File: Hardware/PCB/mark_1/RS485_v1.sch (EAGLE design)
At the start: 4 parts

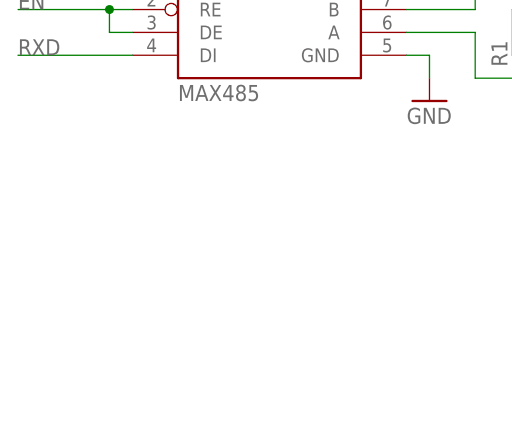
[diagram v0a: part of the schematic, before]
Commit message: 
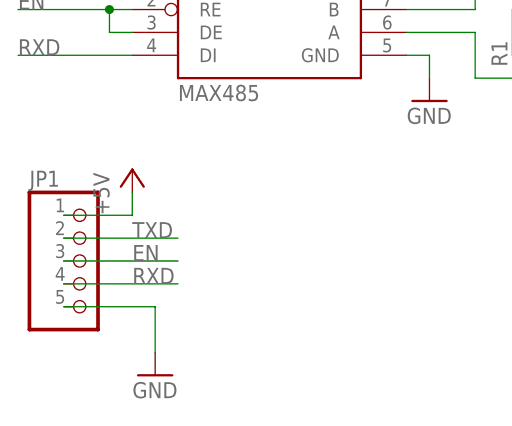
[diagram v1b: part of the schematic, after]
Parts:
- added JP1: (no value), mark_1:PINHD-1X5
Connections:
- net +5V: now also JP1.1
- net EN: now also JP1.3
- net GND: now also JP1.5
- net RXD: now also JP1.4
- net TXD: now also JP1.2
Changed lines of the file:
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@@
 <part name="C1" library="mark_1" deviceset="C-EU" device="C0805K" value="100nF"/>
 <part name="GND3" library="mark_1" deviceset="GND" device=""/>
+<part name="JP1" library="mark_1" deviceset="PINHD-1X5" device=""/>
+<part name="P+3" library="mark_1" deviceset="+5V" device=""/>
+<part name="GND4" library="mark_1" deviceset="GND" device=""/>
 </parts>
 <sheets>
@@
 <instance part="C1" gate="G$1" x="96.52" y="25.4"/>
 <instance part="GND3" gate="1" x="96.52" y="15.24"/>
+<instance part="JP1" gate="A" x="22.86" y="-2.54"/>
+<instance part="P+3" gate="1" x="27.94" y="7.62"/>
+<instance part="GND4" gate="1" x="30.48" y="-15.24"/>
 </instances>
 <busses>
@@
 <pinref part="C1" gate="G$1" pin="1"/>
 <wire x1="96.52" y1="30.48" x2="96.52" y2="27.94" width="0.1524" layer="91"/>
+</segment>
+<segment>
+<pinref part="P+3" gate="1" pin="+5V"/>
+<wire x1="27.94" y1="5.08" x2="27.94" y2="2.54" width="0.1524" layer="91"/>
+<pinref part="JP1" gate="A" pin="1"/>
+<wire x1="27.94" y1="2.54" x2="20.32" y2="2.54" width="0.1524" layer="91"/>
 </segment>
 </net>
@@
 <wire x1="96.52" y1="20.32" x2="96.52" y2="17.78" width="0.1524" layer="91"/>
 </segment>
+<segment>
+<pinref part="JP1" gate="A" pin="5"/>
+<pinref part="GND4" gate="1" pin="GND"/>
+<wire x1="20.32" y1="-7.62" x2="30.48" y2="-7.62" width="0.1524" layer="91"/>
+<wire x1="30.48" y1="-7.62" x2="30.48" y2="-12.7" width="0.1524" layer="91"/>
+</segment>
 </net>
 <net name="TXD" class="0">
@@
 <label x="15.24" y="27.94" size="1.778" layer="95"/>
 </segment>
+<segment>
+<pinref part="JP1" gate="A" pin="2"/>
+<wire x1="20.32" y1="0" x2="33.02" y2="0" width="0.1524" layer="91"/>
+<label x="27.94" y="0" size="1.778" layer="95"/>
+</segment>
 </net>
 <net name="RXD" class="0">
@@
 <wire x1="27.94" y1="20.32" x2="15.24" y2="20.32" width="0.1524" layer="91"/>
 <label x="15.24" y="20.32" size="1.778" layer="95"/>
+</segment>
+<segment>
+<pinref part="JP1" gate="A" pin="4"/>
+<wire x1="20.32" y1="-5.08" x2="33.02" y2="-5.08" width="0.1524" layer="91"/>
+<label x="27.94" y="-5.08" size="1.778" layer="95"/>
 </segment>
 </net>
@@
 <label x="15.24" y="25.4" size="1.778" layer="95"/>
 </segment>
+<segment>
+<pinref part="JP1" gate="A" pin="3"/>
+<wire x1="20.32" y1="-2.54" x2="33.02" y2="-2.54" width="0.1524" layer="91"/>
+<label x="27.94" y="-2.54" size="1.778" layer="95"/>
+</segment>
 </net>

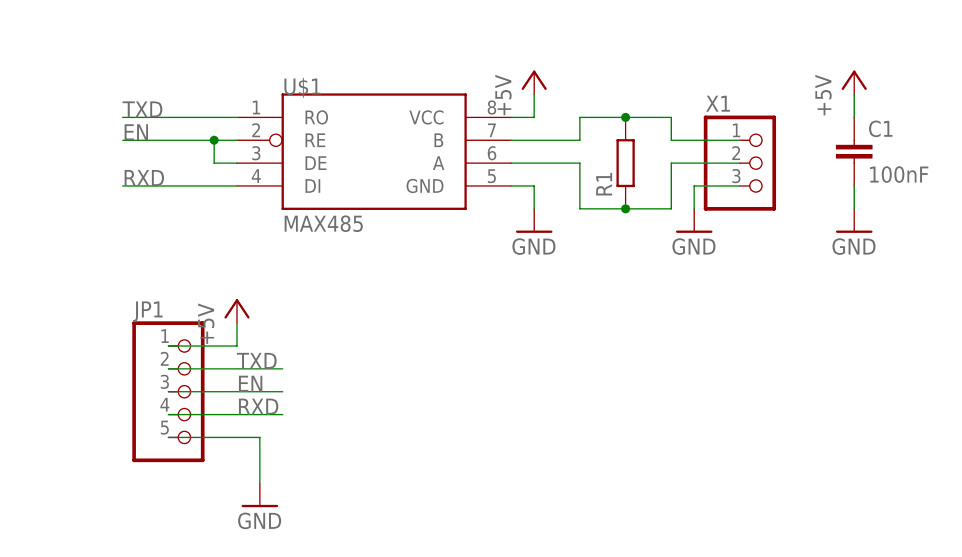
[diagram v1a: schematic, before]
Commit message: 
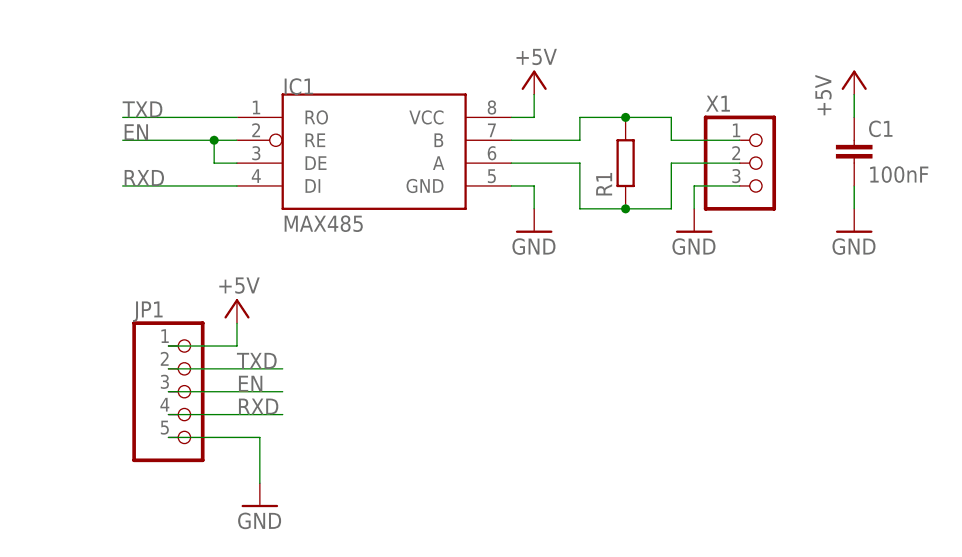
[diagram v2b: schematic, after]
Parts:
- renumbered U$1 to IC1
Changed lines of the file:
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@@
 <part name="P+1" library="mark_1" deviceset="+5V" device=""/>
 <part name="GND1" library="mark_1" deviceset="GND" device=""/>
-<part name="U$1" library="mark_1" deviceset="MAX485" device=""/>
+<part name="IC1" library="mark_1" deviceset="MAX485" device=""/>
 <part name="R1" library="mark_1" deviceset="R-EU_" device="R0805"/>
 <part name="X1" library="mark_1" deviceset="W237-103" device=""/>
@@
 </plain>
 <instances>
-<instance part="P+1" gate="1" x="60.96" y="33.02"/>
+<instance part="P+1" gate="1" x="60.96" y="33.02" smashed="yes">
+<attribute name="VALUE" x="63.5" y="35.56" size="1.778" layer="96" rot="R180"/>
+</instance>
 <instance part="GND1" gate="1" x="60.96" y="15.24"/>
-<instance part="U$1" gate="G$1" x="43.18" y="22.86"/>
+<instance part="IC1" gate="G$1" x="43.18" y="22.86"/>
 <instance part="R1" gate="G$1" x="71.12" y="22.86" rot="R90"/>
 <instance part="X1" gate="G$1" x="86.36" y="22.86"/>
@@
 <instance part="GND3" gate="1" x="96.52" y="15.24"/>
 <instance part="JP1" gate="A" x="22.86" y="-2.54"/>
-<instance part="P+3" gate="1" x="27.94" y="7.62"/>
+<instance part="P+3" gate="1" x="27.94" y="7.62" smashed="yes">
+<attribute name="VALUE" x="30.48" y="10.16" size="1.778" layer="96" rot="R180"/>
+</instance>
 <instance part="GND4" gate="1" x="30.48" y="-15.24"/>
 </instances>
@@
 <net name="+5V" class="0">
 <segment>
-<pinref part="U$1" gate="G$1" pin="VCC"/>
+<pinref part="IC1" gate="G$1" pin="VCC"/>
 <pinref part="P+1" gate="1" pin="+5V"/>
 <wire x1="60.96" y1="30.48" x2="60.96" y2="27.94" width="0.1524" layer="91"/>
@@
 <net name="GND" class="0">
 <segment>
-<pinref part="U$1" gate="G$1" pin="GND"/>
+<pinref part="IC1" gate="G$1" pin="GND"/>
 <pinref part="GND1" gate="1" pin="GND"/>
 <wire x1="60.96" y1="17.78" x2="60.96" y2="20.32" width="0.1524" layer="91"/>
@@
 <net name="TXD" class="0">
 <segment>
-<pinref part="U$1" gate="G$1" pin="RO"/>
+<pinref part="IC1" gate="G$1" pin="RO"/>
 <wire x1="27.94" y1="27.94" x2="15.24" y2="27.94" width="0.1524" layer="91"/>
 <label x="15.24" y="27.94" size="1.778" layer="95"/>
@@
 <net name="RXD" class="0">
 <segment>
-<pinref part="U$1" gate="G$1" pin="DI"/>
+<pinref part="IC1" gate="G$1" pin="DI"/>
 <wire x1="27.94" y1="20.32" x2="15.24" y2="20.32" width="0.1524" layer="91"/>
 <label x="15.24" y="20.32" size="1.778" layer="95"/>
@@
 <wire x1="15.24" y1="25.4" x2="25.4" y2="25.4" width="0.1524" layer="91"/>
 <wire x1="25.4" y1="25.4" x2="25.4" y2="22.86" width="0.1524" layer="91"/>
-<pinref part="U$1" gate="G$1" pin="DE"/>
+<pinref part="IC1" gate="G$1" pin="DE"/>
 <wire x1="25.4" y1="22.86" x2="27.94" y2="22.86" width="0.1524" layer="91"/>
 <junction x="25.4" y="25.4"/>
-<pinref part="U$1" gate="G$1" pin="RE"/>
+<pinref part="IC1" gate="G$1" pin="RE"/>
 <wire x1="27.94" y1="25.4" x2="25.4" y2="25.4" width="0.1524" layer="91"/>
 <label x="15.24" y="25.4" size="1.778" layer="95"/>
@@
 <net name="N$1" class="0">
 <segment>
-<pinref part="U$1" gate="G$1" pin="B"/>
+<pinref part="IC1" gate="G$1" pin="B"/>
 <wire x1="58.42" y1="25.4" x2="66.04" y2="25.4" width="0.1524" layer="91"/>
 <wire x1="66.04" y1="25.4" x2="66.04" y2="27.94" width="0.1524" layer="91"/>
@@
 <net name="N$2" class="0">
 <segment>
-<pinref part="U$1" gate="G$1" pin="A"/>
+<pinref part="IC1" gate="G$1" pin="A"/>
 <wire x1="58.42" y1="22.86" x2="66.04" y2="22.86" width="0.1524" layer="91"/>
 <wire x1="66.04" y1="22.86" x2="66.04" y2="17.78" width="0.1524" layer="91"/>

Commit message: 
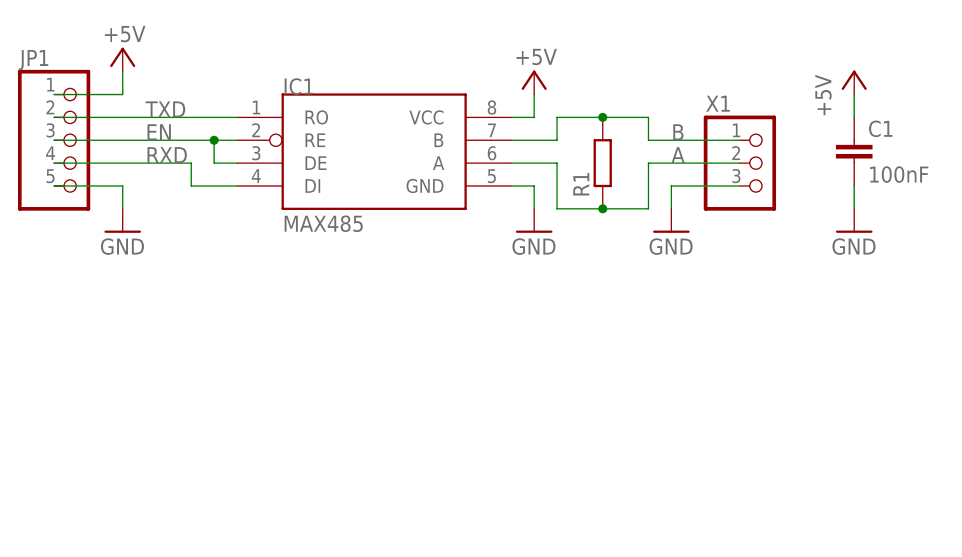
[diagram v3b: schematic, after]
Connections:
- net N$1 renamed B
- net N$2 renamed A
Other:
- moved on the sheet: JP1, R1
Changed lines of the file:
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@@
 <instance part="GND1" gate="1" x="60.96" y="15.24"/>
 <instance part="IC1" gate="G$1" x="43.18" y="22.86"/>
-<instance part="R1" gate="G$1" x="71.12" y="22.86" rot="R90"/>
+<instance part="R1" gate="G$1" x="68.58" y="22.86" rot="R90"/>
 <instance part="X1" gate="G$1" x="86.36" y="22.86"/>
-<instance part="GND2" gate="1" x="78.74" y="15.24"/>
+<instance part="GND2" gate="1" x="76.2" y="15.24"/>
 <instance part="P+2" gate="1" x="96.52" y="33.02"/>
 <instance part="C1" gate="G$1" x="96.52" y="25.4"/>
 <instance part="GND3" gate="1" x="96.52" y="15.24"/>
-<instance part="JP1" gate="A" x="22.86" y="-2.54"/>
-<instance part="P+3" gate="1" x="27.94" y="7.62" smashed="yes">
-<attribute name="VALUE" x="30.48" y="10.16" size="1.778" layer="96" rot="R180"/>
+<instance part="JP1" gate="A" x="10.16" y="25.4"/>
+<instance part="P+3" gate="1" x="15.24" y="35.56" smashed="yes">
+<attribute name="VALUE" x="17.78" y="38.1" size="1.778" layer="96" rot="R180"/>
 </instance>
-<instance part="GND4" gate="1" x="30.48" y="-15.24"/>
+<instance part="GND4" gate="1" x="15.24" y="15.24"/>
 </instances>
 <busses>
@@
 <segment>
 <pinref part="P+3" gate="1" pin="+5V"/>
-<wire x1="27.94" y1="5.08" x2="27.94" y2="2.54" width="0.1524" layer="91"/>
+<wire x1="15.24" y1="33.02" x2="15.24" y2="30.48" width="0.1524" layer="91"/>
 <pinref part="JP1" gate="A" pin="1"/>
-<wire x1="27.94" y1="2.54" x2="20.32" y2="2.54" width="0.1524" layer="91"/>
+<wire x1="15.24" y1="30.48" x2="7.62" y2="30.48" width="0.1524" layer="91"/>
 </segment>
 </net>
@@
 <pinref part="X1" gate="G$1" pin="3"/>
 <pinref part="GND2" gate="1" pin="GND"/>
-<wire x1="78.74" y1="17.78" x2="78.74" y2="20.32" width="0.1524" layer="91"/>
-<wire x1="78.74" y1="20.32" x2="83.82" y2="20.32" width="0.1524" layer="91"/>
+<wire x1="76.2" y1="17.78" x2="76.2" y2="20.32" width="0.1524" layer="91"/>
+<wire x1="76.2" y1="20.32" x2="83.82" y2="20.32" width="0.1524" layer="91"/>
 </segment>
 <segment>
@@
 <pinref part="JP1" gate="A" pin="5"/>
 <pinref part="GND4" gate="1" pin="GND"/>
-<wire x1="20.32" y1="-7.62" x2="30.48" y2="-7.62" width="0.1524" layer="91"/>
-<wire x1="30.48" y1="-7.62" x2="30.48" y2="-12.7" width="0.1524" layer="91"/>
+<wire x1="7.62" y1="20.32" x2="15.24" y2="20.32" width="0.1524" layer="91"/>
+<wire x1="15.24" y1="20.32" x2="15.24" y2="17.78" width="0.1524" layer="91"/>
 </segment>
 </net>
@@
 <segment>
 <pinref part="IC1" gate="G$1" pin="RO"/>
-<wire x1="27.94" y1="27.94" x2="15.24" y2="27.94" width="0.1524" layer="91"/>
-<label x="15.24" y="27.94" size="1.778" layer="95"/>
-</segment>
-<segment>
+<label x="17.78" y="27.94" size="1.778" layer="95"/>
 <pinref part="JP1" gate="A" pin="2"/>
-<wire x1="20.32" y1="0" x2="33.02" y2="0" width="0.1524" layer="91"/>
-<label x="27.94" y="0" size="1.778" layer="95"/>
+<wire x1="27.94" y1="27.94" x2="7.62" y2="27.94" width="0.1524" layer="91"/>
 </segment>
 </net>
@@
 <segment>
 <pinref part="IC1" gate="G$1" pin="DI"/>
-<wire x1="27.94" y1="20.32" x2="15.24" y2="20.32" width="0.1524" layer="91"/>
-<label x="15.24" y="20.32" size="1.778" layer="95"/>
-</segment>
-<segment>
+<wire x1="27.94" y1="20.32" x2="22.86" y2="20.32" width="0.1524" layer="91"/>
+<label x="17.78" y="22.86" size="1.778" layer="95"/>
 <pinref part="JP1" gate="A" pin="4"/>
-<wire x1="20.32" y1="-5.08" x2="33.02" y2="-5.08" width="0.1524" layer="91"/>
-<label x="27.94" y="-5.08" size="1.778" layer="95"/>
+<wire x1="7.62" y1="22.86" x2="22.86" y2="22.86" width="0.1524" layer="91"/>
+<wire x1="22.86" y1="22.86" x2="22.86" y2="20.32" width="0.1524" layer="91"/>
 </segment>
 </net>
 <net name="EN" class="0">
 <segment>
-<wire x1="15.24" y1="25.4" x2="25.4" y2="25.4" width="0.1524" layer="91"/>
 <wire x1="25.4" y1="25.4" x2="25.4" y2="22.86" width="0.1524" layer="91"/>
 <pinref part="IC1" gate="G$1" pin="DE"/>
@@
 <pinref part="IC1" gate="G$1" pin="RE"/>
 <wire x1="27.94" y1="25.4" x2="25.4" y2="25.4" width="0.1524" layer="91"/>
-<label x="15.24" y="25.4" size="1.778" layer="95"/>
-</segment>
-<segment>
+<label x="17.78" y="25.4" size="1.778" layer="95"/>
 <pinref part="JP1" gate="A" pin="3"/>
-<wire x1="20.32" y1="-2.54" x2="33.02" y2="-2.54" width="0.1524" layer="91"/>
-<label x="27.94" y="-2.54" size="1.778" layer="95"/>
+<wire x1="25.4" y1="25.4" x2="7.62" y2="25.4" width="0.1524" layer="91"/>
 </segment>
 </net>
-<net name="N$1" class="0">
+<net name="B" class="0">
 <segment>
 <pinref part="IC1" gate="G$1" pin="B"/>
-<wire x1="58.42" y1="25.4" x2="66.04" y2="25.4" width="0.1524" layer="91"/>
-<wire x1="66.04" y1="25.4" x2="66.04" y2="27.94" width="0.1524" layer="91"/>
+<wire x1="58.42" y1="25.4" x2="63.5" y2="25.4" width="0.1524" layer="91"/>
+<wire x1="63.5" y1="25.4" x2="63.5" y2="27.94" width="0.1524" layer="91"/>
 <pinref part="R1" gate="G$1" pin="2"/>
-<wire x1="66.04" y1="27.94" x2="71.12" y2="27.94" width="0.1524" layer="91"/>
-<wire x1="71.12" y1="27.94" x2="76.2" y2="27.94" width="0.1524" layer="91"/>
-<junction x="71.12" y="27.94"/>
-<wire x1="76.2" y1="27.94" x2="76.2" y2="25.4" width="0.1524" layer="91"/>
+<wire x1="63.5" y1="27.94" x2="68.58" y2="27.94" width="0.1524" layer="91"/>
+<wire x1="68.58" y1="27.94" x2="73.66" y2="27.94" width="0.1524" layer="91"/>
+<junction x="68.58" y="27.94"/>
+<wire x1="73.66" y1="27.94" x2="73.66" y2="25.4" width="0.1524" layer="91"/>
 <pinref part="X1" gate="G$1" pin="1"/>
-<wire x1="76.2" y1="25.4" x2="83.82" y2="25.4" width="0.1524" layer="91"/>
+<wire x1="73.66" y1="25.4" x2="83.82" y2="25.4" width="0.1524" layer="91"/>
+<label x="76.2" y="25.4" size="1.778" layer="95"/>
 </segment>
 </net>
-<net name="N$2" class="0">
+<net name="A" class="0">
 <segment>
 <pinref part="IC1" gate="G$1" pin="A"/>
-<wire x1="58.42" y1="22.86" x2="66.04" y2="22.86" width="0.1524" layer="91"/>
-<wire x1="66.04" y1="22.86" x2="66.04" y2="17.78" width="0.1524" layer="91"/>
+<wire x1="58.42" y1="22.86" x2="63.5" y2="22.86" width="0.1524" layer="91"/>
+<wire x1="63.5" y1="22.86" x2="63.5" y2="17.78" width="0.1524" layer="91"/>
 <pinref part="R1" gate="G$1" pin="1"/>
-<wire x1="66.04" y1="17.78" x2="71.12" y2="17.78" width="0.1524" layer="91"/>
-<wire x1="71.12" y1="17.78" x2="76.2" y2="17.78" width="0.1524" layer="91"/>
-<junction x="71.12" y="17.78"/>
-<wire x1="76.2" y1="17.78" x2="76.2" y2="22.86" width="0.1524" layer="91"/>
+<wire x1="63.5" y1="17.78" x2="68.58" y2="17.78" width="0.1524" layer="91"/>
+<wire x1="68.58" y1="17.78" x2="73.66" y2="17.78" width="0.1524" layer="91"/>
+<junction x="68.58" y="17.78"/>
+<wire x1="73.66" y1="17.78" x2="73.66" y2="22.86" width="0.1524" layer="91"/>
 <pinref part="X1" gate="G$1" pin="2"/>
-<wire x1="76.2" y1="22.86" x2="83.82" y2="22.86" width="0.1524" layer="91"/>
+<wire x1="73.66" y1="22.86" x2="83.82" y2="22.86" width="0.1524" layer="91"/>
+<label x="76.2" y="22.86" size="1.778" layer="95"/>
 </segment>
 </net>
